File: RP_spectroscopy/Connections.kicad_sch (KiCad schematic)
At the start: 37 parts, among them J1 Extension connector 1, J10 Conn_Coaxial, J2 Extension connector 2, J3 Conn_Coaxial, J4 Conn_Coaxial, J5 Conn_Coaxial, J6 Conn_Coaxial, J7 Molex PicoBlade, J8 Molex PicoBlade, J9 Conn_Coaxial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

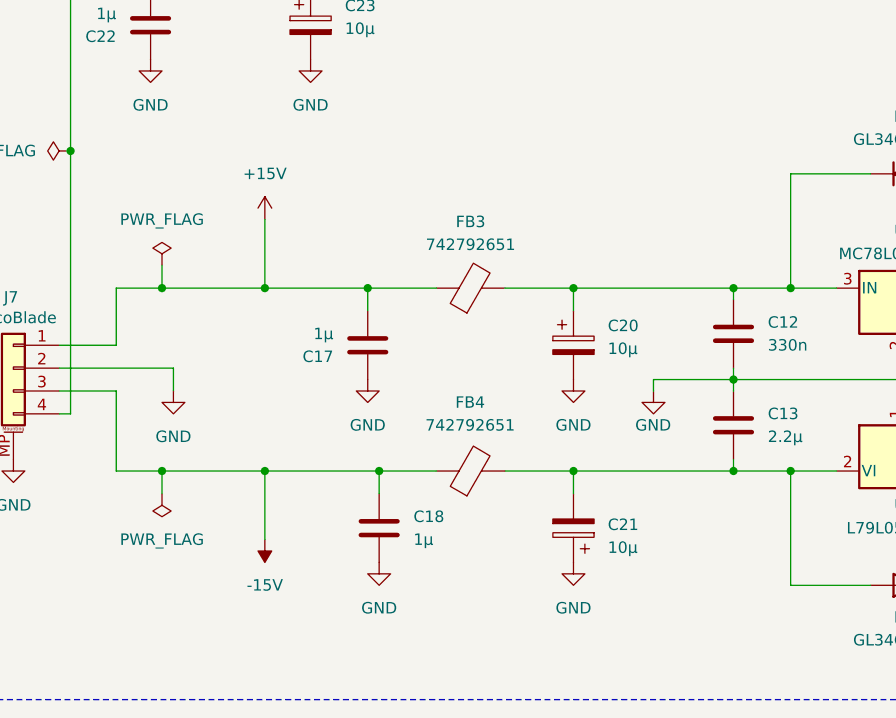
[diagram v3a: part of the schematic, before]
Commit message: Continued with the wireing of the PCB
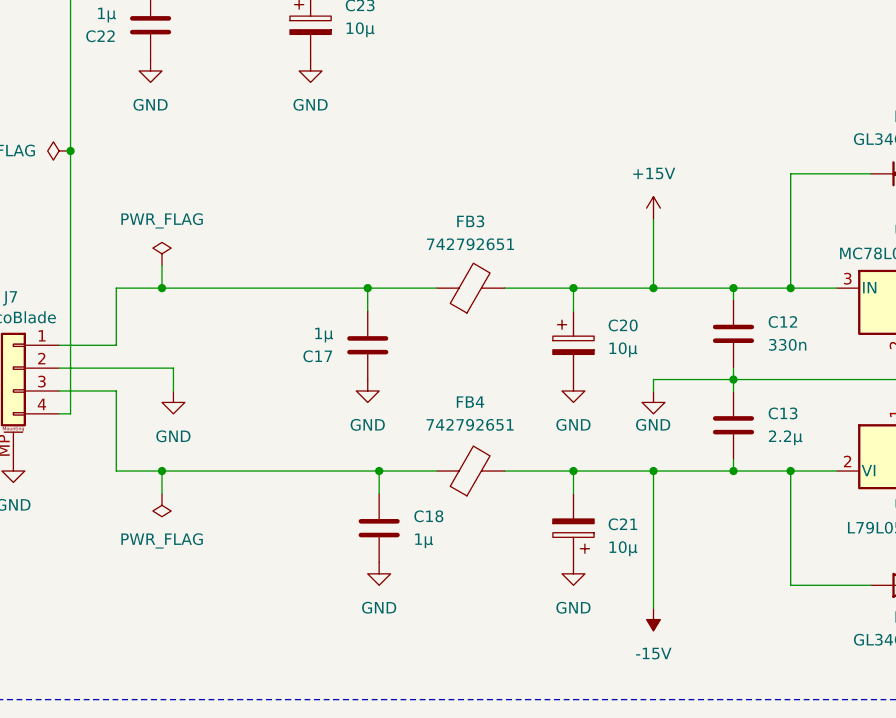
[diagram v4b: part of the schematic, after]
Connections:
- net +15V: now also C12.1, C20.1, D2.1 (K), FB3.2, U4.3 (IN); no longer C17.2, FB3.1, J7.1 (Pin_1)
- net -15V: now also C13.2, C21.2, D3.2 (A), FB4.2, U5.2 (VI); no longer C18.1, FB4.1, J7.3 (Pin_3)
- new net: C18.1, FB4.1, J7.3 (Pin_3)
- new net: C17.2, FB3.1, J7.1 (Pin_1)
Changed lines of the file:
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@@
 	)
 	(junction
-		(at 55.88 160.02)
-		(diameter 0)
-		(color 0 0 0 0)
-	)
-	(junction
 		(at 144.78 139.7)
 		(diameter 0)
@@
 	)
 	(junction
-		(at 55.88 139.7)
-		(diameter 0)
-		(color 0 0 0 0)
-	)
-	(junction
 		(at 127 149.86)
 		(diameter 0)
@@
 	)
 	(junction
+		(at 99.06 139.7)
+		(diameter 0)
+		(color 0 0 0 0)
+	)
+	(junction
 		(at 44.45 139.7)
 		(diameter 0)
@@
 	)
 	(junction
+		(at 99.06 160.02)
+		(diameter 0)
+		(color 0 0 0 0)
+	)
+	(junction
 		(at 30.48 53.34)
 		(diameter 0)
@@
 	(wire
 		(pts
+			(xy 99.06 160.02) (xy 99.06 175.26)
+		)
+		(stroke
+			(width 0)
+			(type default)
+		)
+	)
+	(wire
+		(pts
 			(xy 91.44 27.94) (xy 86.36 27.94)
 		)
@@
 	(wire
 		(pts
+			(xy 99.06 160.02) (xy 107.95 160.02)
+		)
+		(stroke
+			(width 0)
+			(type default)
+		)
+	)
+	(wire
+		(pts
 			(xy 149.86 25.4) (xy 152.4 25.4)
 		)
@@
 	(wire
 		(pts
-			(xy 55.88 139.7) (xy 67.31 139.7)
-		)
-		(stroke
-			(width 0)
-			(type default)
-		)
-	)
-	(wire
-		(pts
-			(xy 55.88 160.02) (xy 55.88 167.64)
+			(xy 44.45 139.7) (xy 67.31 139.7)
 		)
 		(stroke
@@
 	(wire
 		(pts
-			(xy 55.88 139.7) (xy 44.45 139.7)
-		)
-		(stroke
-			(width 0)
-			(type default)
-		)
-	)
-	(wire
-		(pts
 			(xy 33.02 146.05) (xy 39.37 146.05)
 		)
@@
 	(wire
 		(pts
-			(xy 55.88 160.02) (xy 68.58 160.02)
+			(xy 44.45 160.02) (xy 68.58 160.02)
 		)
 		(stroke
@@
 	(wire
 		(pts
-			(xy 55.88 132.08) (xy 55.88 139.7)
-		)
-		(stroke
-			(width 0)
-			(type default)
-		)
-	)
-	(wire
-		(pts
 			(xy 34.29 153.67) (xy 33.02 153.67)
 		)
@@
 	(wire
 		(pts
+			(xy 99.06 139.7) (xy 107.95 139.7)
+		)
+		(stroke
+			(width 0)
+			(type default)
+		)
+	)
+	(wire
+		(pts
 			(xy 255.27 147.32) (xy 255.27 146.05)
 		)
@@
 	(wire
 		(pts
-			(xy 90.17 139.7) (xy 107.95 139.7)
+			(xy 90.17 139.7) (xy 99.06 139.7)
 		)
 		(stroke
@@
 	(wire
 		(pts
+			(xy 99.06 132.08) (xy 99.06 139.7)
+		)
+		(stroke
+			(width 0)
+			(type default)
+		)
+	)
+	(wire
+		(pts
 			(xy 59.69 62.23) (xy 59.69 68.58)
 		)
@@
 	(wire
 		(pts
-			(xy 90.17 160.02) (xy 107.95 160.02)
+			(xy 90.17 160.02) (xy 99.06 160.02)
 		)
 		(stroke
@@
 	(wire
 		(pts
-			(xy 44.45 160.02) (xy 55.88 160.02)
-		)
-		(stroke
-			(width 0)
-			(type default)
-		)
-	)
-	(wire
-		(pts
 			(xy 74.93 160.02) (xy 68.58 160.02)
 		)
@@
 	(symbol
 		(lib_id "power:+15V")
-		(at 55.88 132.08 0)
+		(at 99.06 132.08 0)
 		(unit 1)
 		(exclude_from_sim no)
@@
 		(fields_autoplaced yes)
 		(property "Reference" "#PWR037"
-			(at 55.88 135.89 0)
+			(at 99.06 135.89 0)
 			(effects
 				(font
@@
 		)
 		(property "Value" "+15V"
-			(at 55.88 127 0)
+			(at 99.06 127 0)
 			(effects
 				(font
@@
 		)
 		(property "Footprint" ""
-			(at 55.88 132.08 0)
+			(at 99.06 132.08 0)
 			(effects
 				(font
@@
 		)
 		(property "Datasheet" ""
-			(at 55.88 132.08 0)
+			(at 99.06 132.08 0)
 			(effects
 				(font
@@
 		)
 		(property "Description" "Power symbol creates a global label with name \"+15V\""
-			(at 55.88 132.08 0)
+			(at 99.06 132.08 0)
 			(effects
 				(font
@@
 	(symbol
 		(lib_id "power:-15V")
-		(at 55.88 167.64 180)
+		(at 99.06 175.26 180)
 		(unit 1)
 		(exclude_from_sim no)
@@
 		(fields_autoplaced yes)
 		(property "Reference" "#PWR038"
-			(at 55.88 163.83 0)
+			(at 99.06 171.45 0)
 			(effects
 				(font
@@
 		)
 		(property "Value" "-15V"
-			(at 55.88 172.72 0)
+			(at 99.06 180.34 0)
 			(effects
 				(font
@@
 		)
 		(property "Footprint" ""
-			(at 55.88 167.64 0)
+			(at 99.06 175.26 0)
 			(effects
 				(font
@@
 		)
 		(property "Datasheet" ""
-			(at 55.88 167.64 0)
+			(at 99.06 175.26 0)
 			(effects
 				(font
@@
 		)
 		(property "Description" "Power symbol creates a global label with name \"-15V\""
-			(at 55.88 167.64 0)
+			(at 99.06 175.26 0)
 			(effects
 				(font

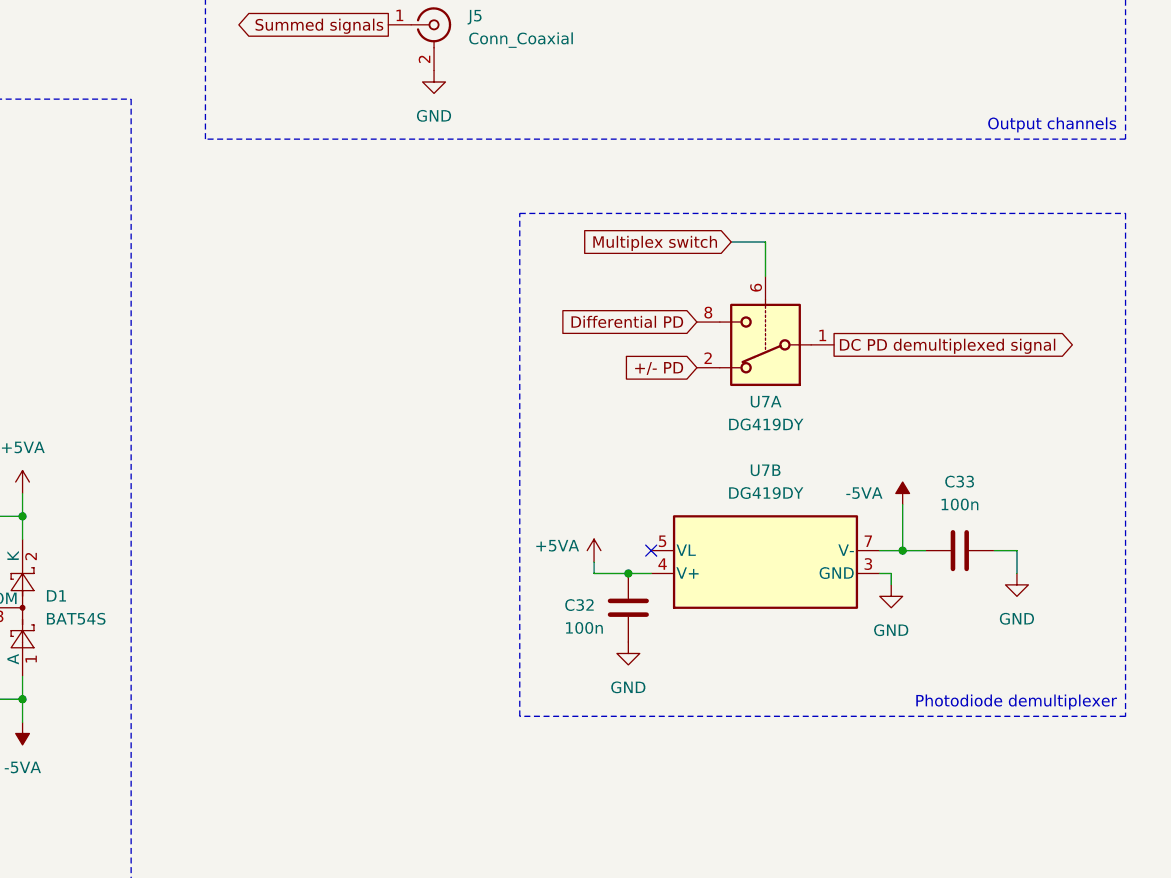
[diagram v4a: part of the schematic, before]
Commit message: Added the BP filter and the amplification stages. It should be done.
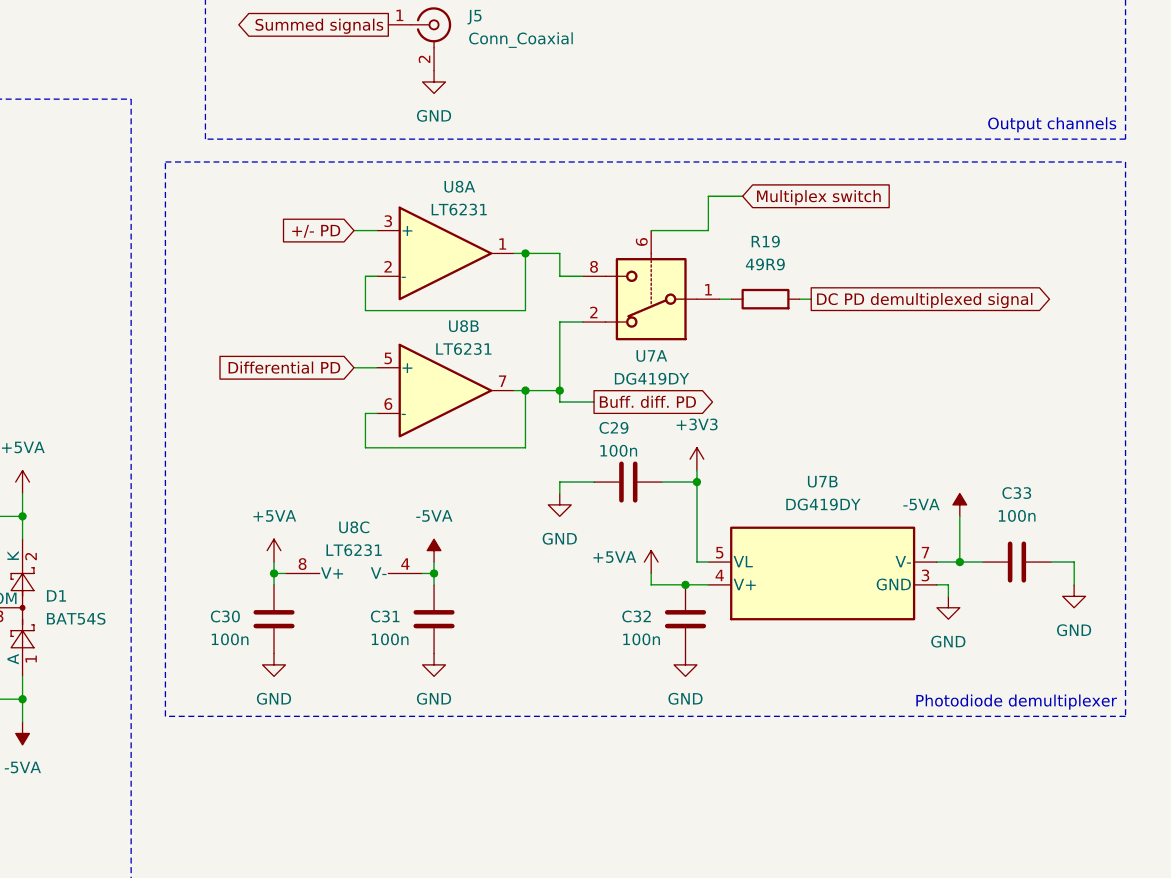
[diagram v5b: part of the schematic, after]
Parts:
- added C29, C30, C31: 100n, Capacitor_SMD:C_0805_2012Metric_Pad1.18x1.45mm_HandSolder, symbol Device:C
- added R19: 49R9, Resistor_SMD:R_0805_2012Metric_Pad1.20x1.40mm_HandSolder, symbol Device:R
- added U8: LT6231, Package_SO:SOIC-8_3.9x4.9mm_P1.27mm, symbol Amplifier_Operational:LT6234
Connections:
- net +3V3: now also U7.5 (VL), C29.1
- net +5VA: now also C30.1, U8.8 (V+)
- net +/- PD: now also U8.3 (+); no longer U7.2
- net -5VA: now also C31.1, U8.4 (V-)
- net DC PD demultiplexed signal: now also R19.2; no longer U7.1
- net Differential PD: now also U8.5 (+); no longer U7.8
- net GND: now also C29.2, C30.2, C31.2
- new net: U7.8, U8.1, U8.2 (-)
- new net: R19.1, U7.1
- new net Buff. diff. PD: U7.2, U8.6 (-), U8.7
- no-connect marks 7 -> 6
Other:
- moved on the sheet: C32, C33, U7A, U7B
